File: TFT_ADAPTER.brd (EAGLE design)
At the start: 16.2 x 33.1 mm, 0 parts

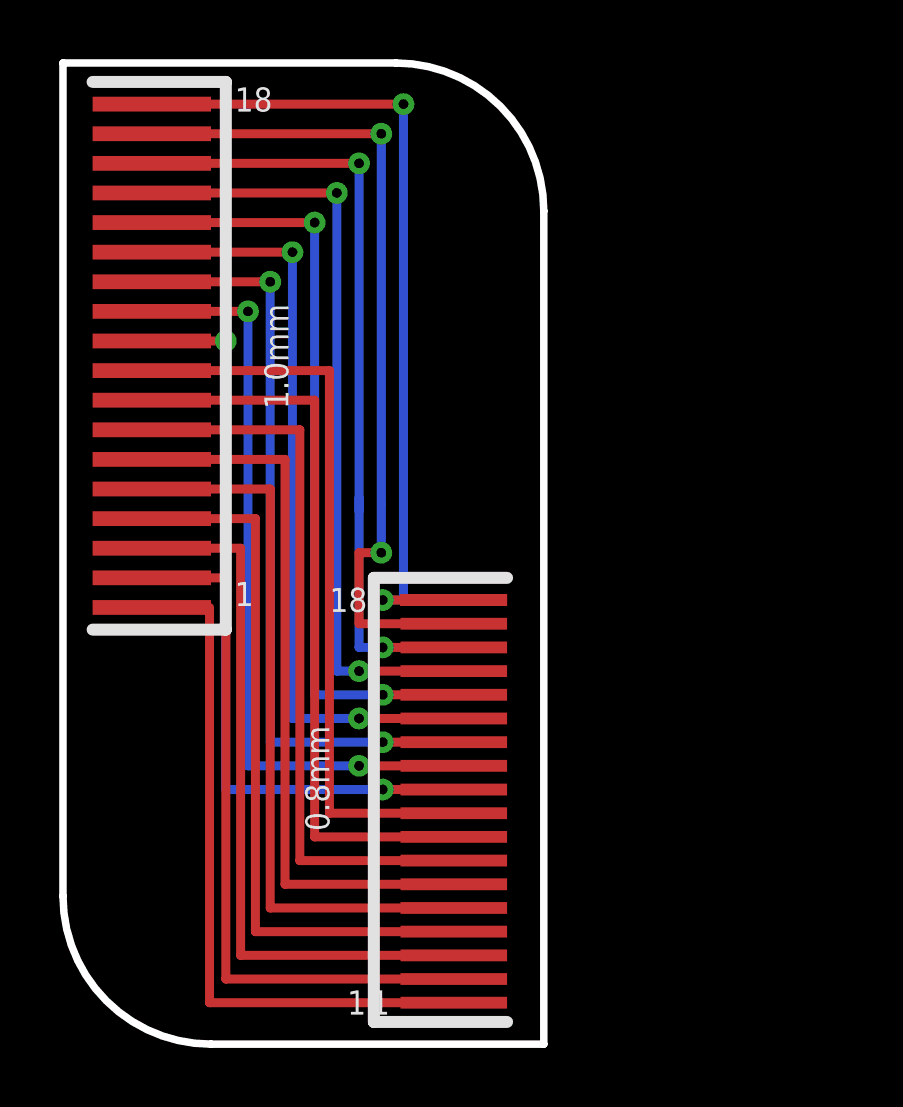
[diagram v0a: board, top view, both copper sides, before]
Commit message: new TFT adapter
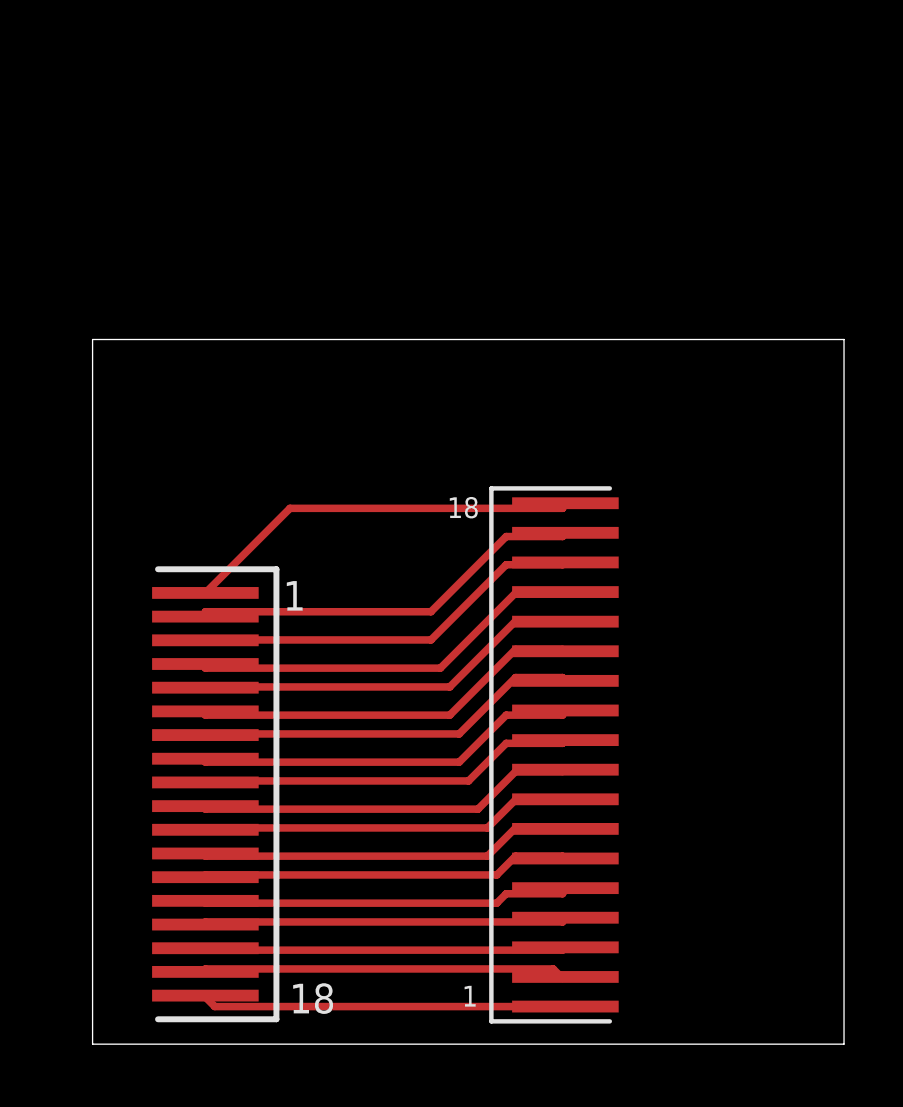
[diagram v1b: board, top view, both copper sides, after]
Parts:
- added U$1: FCC-18-1.0MM, custom:FFC-18-1.0MM
- added U$2: FCC-18-0.8MM, custom:FFC-18-0.8MM
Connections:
- new net N$1: U$1.P$18, U$2.P$1
- new net N$10: U$1.P$9, U$2.P$10
- new net N$11: U$1.P$8, U$2.P$11
- new net N$12: U$1.P$7, U$2.P$12
- new net N$13: U$1.P$6, U$2.P$13
- new net N$14: U$1.P$5, U$2.P$14
- new net N$15: U$1.P$4, U$2.P$15
- new net N$16: U$1.P$3, U$2.P$16
- new net N$17: U$1.P$2, U$2.P$17
- new net N$18: U$1.P$1, U$2.P$18
- new net N$2: U$1.P$17, U$2.P$2
- new net N$3: U$1.P$16, U$2.P$3
- new net N$4: U$1.P$15, U$2.P$4
- new net N$5: U$1.P$14, U$2.P$5
- new net N$6: U$1.P$13, U$2.P$6
- new net N$7: U$1.P$12, U$2.P$7
- new net N$8: U$1.P$11, U$2.P$8
- new net N$9: U$1.P$10, U$2.P$9
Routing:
- net S$9: track 21.8 -> 0.00 mm
- net S$24: track 20.6 -> 0.00 mm, vias 1 -> 0
- net S$3: track 20.6 -> 0.00 mm
- net S$23: track 19.7 -> 0.00 mm, vias 1 -> 0
- net S$22: track 19.0 -> 0.00 mm, vias 1 -> 0
- net S$8: track 18.5 -> 0.00 mm
- net S$26: track 18.2 -> 0.00 mm, vias 1 -> 0
- net S$7: track 17.8 -> 0.00 mm
- net S$21: track 17.8 -> 0.00 mm, vias 1 -> 0
- net S$35: track 17.8 -> 0.00 mm, vias 1 -> 0
- net S$6: track 17.1 -> 0.00 mm
- net S$19: track 16.9 -> 0.00 mm, vias 1 -> 0
- net S$25: track 16.8 -> 0.00 mm, vias 1 -> 0
- net S$5: track 16.6 -> 0.00 mm
- net S$1: track 15.9 -> 0.00 mm, vias 1 -> 0
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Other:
- board size 16.2 x 33.1 mm -> 25.4 x 23.8 mm
- board text removed: "0.8mm"
- board text removed: "1"
- board text removed: "1.0mm"
- board text removed: "18"
- board text removed: "Ryzee119 2016"
